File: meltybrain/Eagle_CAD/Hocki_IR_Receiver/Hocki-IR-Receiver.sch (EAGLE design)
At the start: 67 parts, among them U1 OPA2380AIDGKR, U10 LMH6612MAX/NOPB, U11 LMH6612MAX/NOPB, U2 OPA2380AIDGKR, U3 TLV3502AIDCNR, U4 TLV3502AIDCNR, U5 SN74LVC1G58DCKR, U6 NL27WZ32USG, U7 TMUX1204DGSR, U8 LP38693MP-5.0/NOPB, U9 TLV73310PDBVT

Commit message: progress...
IR receiver has all parts accounting BoM
started doing that for control
progress on control layout
Varun I hate this...
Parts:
- removed C4, C5: 50n, rcl:C-USC0603
- removed R5: 50, resistor:R-US_R0603
- C1: value 50n -> 47n; device rcl:C-USC0603 -> rcl:C-USC1206
- C2: value 0.5p -> 47n; device rcl:C-USC0603 -> rcl:C-USC1206
- C3: value 2p -> 47n; device rcl:C-USC0603 -> rcl:C-USC1206
- R1: device resistor:R-US_R0603 -> rcl:R-US_R1206
- R10, R11, R16, R21, R28, R29, R3, R30, R31, R4: value 500 -> 499
- R14, R15, R7: value 30k -> 31.6k
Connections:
- removed net N$11: C3.2, R13.1, R9.2, U2.OUTB
- removed net N$8: C2.2, R12.1, R8.2, U2.OUTA
- new net N$21: D1.A, R6.2
- net 100KGAIN: now also R12.1, R8.2, U2.OUTA; no longer D2.A, R12.2
- net 100KPEAK: now also C2.1; no longer C4.1
- net 10KGAIN: now also R13.1, R9.2, U2.OUTB; no longer D3.A, R13.2
- net 10KPEAK: now also C3.1; no longer C5.1
- net 10MGAIN: now also R1.2, U1.OUTA; no longer R5.2
- net 1MGAIN: now also R2.2, R6.1, U1.OUTB; no longer D1.A, R6.2
- net GND: now also C2.2, C3.2; no longer C4.2, C5.2
- net N$10: no longer C3.1
- net N$2: now also D2.A, R12.2; no longer R1.2, R5.1, U1.OUTA
- net N$4: now also D3.A, R13.2; no longer R2.2, R6.1, U1.OUTB
- net N$6: no longer C2.1
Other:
- moved on the sheet: C2, C3

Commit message: added IR connectors
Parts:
- added C4: 100p, rcl:C-USC0603
- added J1: SM05B-SRSS-TB(LF)(SN), Hocki_Library:SM05B-SRSS-TB(LF)(SN)
- C7: value 1u -> 2.2u
- U8: value LP38693MP-5.0/NOPB -> AP2210K-5.0TRG1; device Hocki_Library:LP38693MP-5.0/NOPB -> Hocki_Library:AP2210K-5.0TRG1
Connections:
- removed net VIN: C6.1, U8.EN, U8.VIN
- new net 9V: C6.1, J1.1, U8.EN, U8.IN
- new net N$8: C4.1, U8.BYP
- net 5V: now also J1.SHIELD, U8.OUT; no longer U8.VOUT
- net A0: now also J1.3
- net A1: now also J1.4
- net GND: now also C4.2, J1.5
- net VG_SIGNAL: now also J1.2

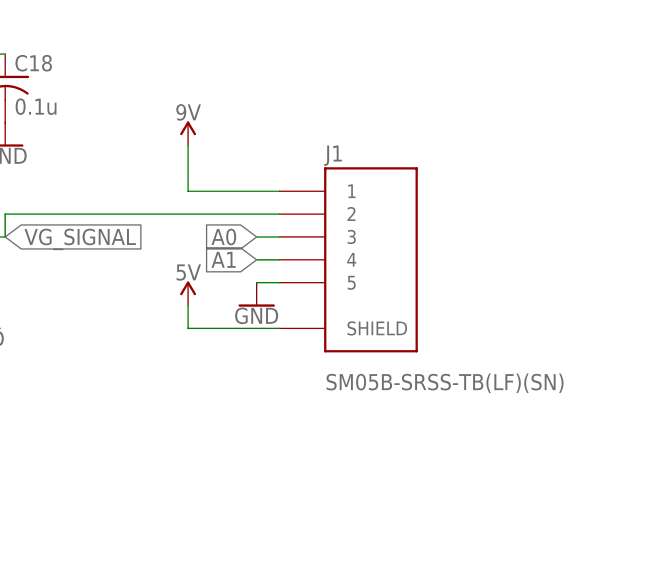
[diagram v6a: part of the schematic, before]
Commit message: 5 to 3 pin connector
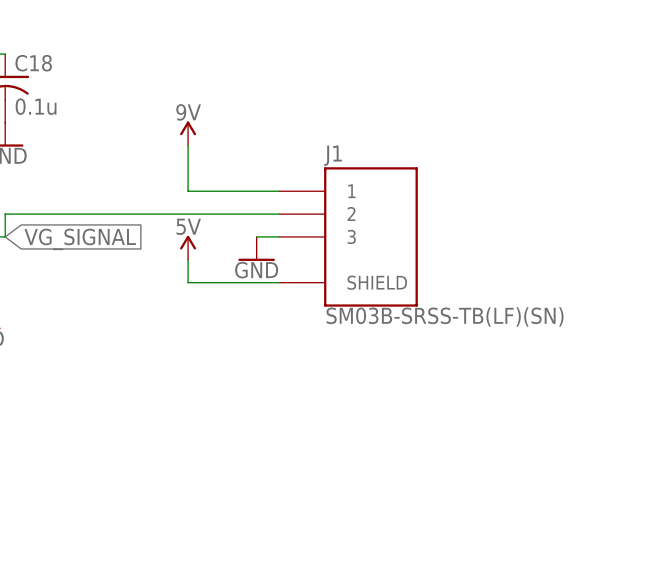
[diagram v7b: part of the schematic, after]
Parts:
- J1: value SM05B-SRSS-TB(LF)(SN) -> SM03B-SRSS-TB(LF)(SN); device Hocki_Library:SM05B-SRSS-TB(LF)(SN) -> Hocki_Library:SM03B-SRSS-TB(LF)(SN)
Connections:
- net A0: no longer J1.3
- net A1: no longer J1.4
- net GND: now also J1.3; no longer J1.5
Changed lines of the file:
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@@
 <part name="C4" library="rcl" library_urn="urn:adsk.eagle:library:334" deviceset="C-US" device="C0603" package3d_urn="urn:adsk.eagle:package:23616/2" value="100p"/>
 <part name="GND33" library="SparkFun-PowerSymbols" library_urn="urn:adsk.eagle:library:530" deviceset="GND" device=""/>
-<part name="J1" library="Hocki_Library" deviceset="SM05B-SRSS-TB(LF)(SN)" device=""/>
 <part name="SUPPLY12" library="Hocki_Library" deviceset="9V" device=""/>
 <part name="SUPPLY17" library="Hocki_Library" deviceset="9V" device=""/>
 <part name="GND34" library="SparkFun-PowerSymbols" library_urn="urn:adsk.eagle:library:530" deviceset="GND" device=""/>
 <part name="SUPPLY18" library="SparkFun-PowerSymbols" library_urn="urn:adsk.eagle:library:530" deviceset="5V" device=""/>
+<part name="J1" library="Hocki_Library" deviceset="SM03B-SRSS-TB(LF)(SN)" device=""/>
 </parts>
 <sheets>
@@
 <attribute name="VALUE" x="-30.48" y="63.246" size="1.778" layer="96" align="top-center"/>
 </instance>
-<instance part="J1" gate="G$1" x="347.98" y="5.08" smashed="yes">
-<attribute name="NAME" x="342.9" y="16.002" size="1.778" layer="95"/>
-<attribute name="VALUE" x="342.9" y="-7.62" size="1.778" layer="96" align="top-left"/>
-</instance>
 <instance part="SUPPLY12" gate="G$1" x="-63.5" y="91.44" smashed="yes">
 <attribute name="VALUE" x="-63.5" y="94.234" size="1.778" layer="96" align="bottom-center"/>
@@
 <attribute name="VALUE" x="327.66" y="20.574" size="1.778" layer="96" align="bottom-center"/>
 </instance>
-<instance part="GND34" gate="1" x="335.28" y="0" smashed="yes">
-<attribute name="VALUE" x="335.28" y="-0.254" size="1.778" layer="96" align="top-center"/>
-</instance>
-<instance part="SUPPLY18" gate="G$1" x="327.66" y="0" smashed="yes">
-<attribute name="VALUE" x="327.66" y="2.794" size="1.778" layer="96" align="bottom-center"/>
+<instance part="GND34" gate="1" x="335.28" y="5.08" smashed="yes">
+<attribute name="VALUE" x="335.28" y="4.826" size="1.778" layer="96" align="top-center"/>
+</instance>
+<instance part="SUPPLY18" gate="G$1" x="327.66" y="5.08" smashed="yes">
+<attribute name="VALUE" x="327.66" y="7.874" size="1.778" layer="96" align="bottom-center"/>
+</instance>
+<instance part="J1" gate="G$1" x="347.98" y="7.62" smashed="yes">
+<attribute name="NAME" x="342.9" y="16.002" size="1.778" layer="95"/>
+<attribute name="VALUE" x="342.9" y="-0.254" size="1.778" layer="96" align="top-left"/>
 </instance>
 </instances>
@@
 </segment>
 <segment>
-<pinref part="J1" gate="G$1" pin="5"/>
-<wire x1="337.82" y1="2.54" x2="335.28" y2="2.54" width="0.1524" layer="91"/>
 <pinref part="GND34" gate="1" pin="GND"/>
+<pinref part="J1" gate="G$1" pin="3"/>
+<wire x1="337.82" y1="7.62" x2="335.28" y2="7.62" width="0.1524" layer="91"/>
 </segment>
 </net>
@@
 </segment>
 <segment>
+<wire x1="337.82" y1="2.54" x2="327.66" y2="2.54" width="0.1524" layer="91"/>
+<pinref part="SUPPLY18" gate="G$1" pin="5V"/>
+<wire x1="327.66" y1="2.54" x2="327.66" y2="5.08" width="0.1524" layer="91"/>
 <pinref part="J1" gate="G$1" pin="SHIELD"/>
-<wire x1="337.82" y1="-2.54" x2="327.66" y2="-2.54" width="0.1524" layer="91"/>
-<pinref part="SUPPLY18" gate="G$1" pin="5V"/>
-<wire x1="327.66" y1="-2.54" x2="327.66" y2="0" width="0.1524" layer="91"/>
 </segment>
 </net>
@@
 <label x="266.7" y="0" size="1.778" layer="95" rot="R180" xref="yes"/>
 </segment>
-<segment>
-<pinref part="J1" gate="G$1" pin="4"/>
-<wire x1="337.82" y1="5.08" x2="335.28" y2="5.08" width="0.1524" layer="91"/>
-<label x="335.28" y="5.08" size="1.778" layer="95" rot="R180" xref="yes"/>
-</segment>
 </net>
 <net name="A0" class="0">
@@
 <wire x1="269.24" y1="2.54" x2="266.7" y2="2.54" width="0.1524" layer="91"/>
 <label x="266.7" y="2.54" size="1.778" layer="95" rot="R180" xref="yes"/>
-</segment>
-<segment>
-<pinref part="J1" gate="G$1" pin="3"/>
-<wire x1="337.82" y1="7.62" x2="335.28" y2="7.62" width="0.1524" layer="91"/>
-<label x="335.28" y="7.62" size="1.778" layer="95" rot="R180" xref="yes"/>
 </segment>
 </net>
@@
 <wire x1="302.26" y1="7.62" x2="307.34" y2="7.62" width="0.1524" layer="91"/>
 <label x="307.34" y="7.62" size="1.778" layer="95" xref="yes"/>
-<pinref part="J1" gate="G$1" pin="2"/>
 <wire x1="337.82" y1="10.16" x2="307.34" y2="10.16" width="0.1524" layer="91"/>
 <wire x1="307.34" y1="10.16" x2="307.34" y2="7.62" width="0.1524" layer="91"/>
+<pinref part="J1" gate="G$1" pin="2"/>
 </segment>
 </net>
@@
 </segment>
 <segment>
-<pinref part="J1" gate="G$1" pin="1"/>
 <wire x1="337.82" y1="12.7" x2="327.66" y2="12.7" width="0.1524" layer="91"/>
 <wire x1="327.66" y1="12.7" x2="327.66" y2="17.78" width="0.1524" layer="91"/>
 <pinref part="SUPPLY17" gate="G$1" pin="9V"/>
-</segment>
-</net>
+<pinref part="J1" gate="G$1" pin="1"/>
+</segment>
+</net>

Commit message: IR board 100%...again
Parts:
- removed C18: 0.1u, rcl:C-USC0603
- added C5: 47nF, rcl:C-USC1206
- added D8, D9: GREEN, SparkFun-LED:LED-GREEN0603
- added R32: 300, resistor:R-US_R0603
- added R5: 10M, rcl:R-US_R1206
- C1, C2: value 47n -> 1uF; device rcl:C-USC1206 -> rcl:C-USC0603
- C10: value 1u -> 2.2uF
- C11, C6: value 1u -> 1uF
- C12: value 0.1u -> 1uF
- C13, C14, C15, C16, C17: value 0.1u -> 0.1uF
- C3: value 47n -> 47nF
- C4: value 100p -> 47nF; device rcl:C-USC0603 -> rcl:C-USC1206
- C7: value 2.2u -> 100pF
- C8, C9: value 1u -> 0.1uF
- D1, D2, D3: value RB521S30T1G -> TEFD4300F; device Hocki_Library:RB521S30T1G -> Hocki_Library:TEFD4300F
- D5, D6, D7: value TEFD4300F -> RB521S30T1G; device Hocki_Library:TEFD4300F -> Hocki_Library:RB521S30T1G
- R1: value 10M -> 499; device rcl:R-US_R1206 -> resistor:R-US_R0603
- R10, R11: value 499 -> 49.9
- R12, R13: value 50 -> 31.6k
- R15: value 31.6k -> 499
- R16: value 499 -> 100
- R17: value 100 -> 30
- R18: value 300 -> 30
- R19: value 100 -> 300
- R2: value 1M -> 499
- R20: value 300 -> 100
- R21: value 499 -> 30
- R22: value 10k -> 300
- R25: value 30 -> 10k
- R26, R27: value 30 -> 499
- R6: value 50 -> 1M
- R7: value 31.6k -> 100k
- R8: value 100k -> 10k
- R9: value 10k -> 49.9
- U10: value LMH6612MAX/NOPB -> NL27WZ32USG; device Hocki_Library:LMH6612MAX/NOPB -> Hocki_Library:NL27WZ32USG
- U11: value LMH6612MAX/NOPB -> TMUX1204DGSR; device Hocki_Library:LMH6612MAX/NOPB -> Hocki_Library:TMUX1204DGSR
- U3: value TLV3502AIDCNR -> AP2210K-5.0TRG1; device Hocki_Library:TLV3502AIDCNR -> Hocki_Library:AP2210K-5.0TRG1
- U4: value TLV3502AIDCNR -> LMH6612MAX/NOPB; device Hocki_Library:TLV3502AIDCNR -> Hocki_Library:LMH6612MAX/NOPB
- U5: value SN74LVC1G58DCKR -> LMH6612MAX/NOPB; device Hocki_Library:SN74LVC1G58DCKR -> Hocki_Library:LMH6612MAX/NOPB
- U6: value NL27WZ32USG -> TLV73310PDBVT; device Hocki_Library:NL27WZ32USG -> Hocki_Library:TLV73310PDBVT
- U7: value TMUX1204DGSR -> TLV3502AIDCNR; device Hocki_Library:TMUX1204DGSR -> Hocki_Library:TLV3502AIDCNR
- U8: value AP2210K-5.0TRG1 -> TLV3502AIDCNR; device Hocki_Library:AP2210K-5.0TRG1 -> Hocki_Library:TLV3502AIDCNR
- U9: value TLV73310PDBVT -> SN74LVC1G58DCKR; device Hocki_Library:TLV73310PDBVT -> Hocki_Library:SN74LVC1G58DCKR
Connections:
- new net N$11: D9.C, R32.2
- new net N$24: D8.C, R31.2
- net 1.0V: now also C12.1, R1.2, R16.2, R20.2, U6.OUT; no longer C9.1, R10.2, R17.2, R19.2, U9.OUT
- net 100KGAIN: now also R11.1, R7.2, U11.S3; no longer R12.1, R8.2, U7.S3
- net 100KLOGIC: now also U10.B1, U7.OUTB, U9.IN1; no longer U3.OUTB, U5.IN1, U6.B1
- net 100KPEAK: now also C4.1, D6.C, R13.2, U4.INB+; no longer C2.1, D2.C, R14.2, U10.INB+
- net 10KGAIN: now also R10.1, R30.2, R8.2, U11.S4; no longer R13.1, R28.2, R9.2, U7.S4
- net 10KLOGIC: now also R25.1, U10.A1, U10.A2, U8.OUTA; no longer R23.1, U4.OUTA, U6.A1, U6.A2
- net 10KPEAK: now also C5.1, D7.C, R14.2, U5.INA+; no longer C3.1, D3.C, R15.2, U11.INA+
- net 10MGAIN: now also R27.2, R5.2, U11.S1; no longer R1.2, R31.2, U7.S1
- net 1MGAIN: now also R28.2, R6.2, R9.1, U11.S2; no longer R2.2, R30.2, R6.1, U7.S2
- net 1MLOGIC: now also R23.1, U7.OUTA, U9.IN2; no longer R22.1, U3.OUTA, U5.IN2
- net 5V: now also C1.1, C2.1, C9.1, D9.A, U10.VCC, U11.EN, U11.VCC, U3.OUT, U5.V+, U6.EN, U6.IN, U7.V+, U8.V+, U9.VCC; no longer C12.1, C18.1, C7.1, U10.V+, U11.V+, U3.V+, U5.VCC, U6.VCC, U7.EN, U7.VCC, U8.OUT, U9.EN, U9.IN
- net 9V: now also D8.A, U3.EN, U3.IN; no longer U8.EN, U8.IN
- net A0: now also U10.Y2, U11.A0; no longer U6.Y2, U7.A0
- net A1: now also U10.Y1, U11.A1; no longer U6.Y1, U7.A1
- net GND: now also C5.2, D1.ANODE, D2.ANODE, D3.ANODE, R12.1, R13.1, R19.1, R2.1, R22.1, R26.1, R27.1, R32.1, U10.GND, U11.GND, U3.GND, U5.INB+, U5.INB-, U5.V-, U7.V-, U8.INB-, U8.V-, U9.IN0; no longer C18.2, D5.ANODE, D6.ANODE, D7.ANODE, R11.1, R16.1, R18.1, R20.1, R21.1, R7.1, U10.V-, U11.INB+, U11.INB-, U11.V-, U3.V-, U4.INB-, U5.GND, U5.IN0, U7.GND, U8.GND
- net N$1: now also D1.CATHODE, R5.1; no longer D4.CATHODE, R1.1
- net N$10: now also D4.CATHODE, R8.1; no longer D7.CATHODE, R9.1
- net N$12: now also R3.1, R4.2; no longer R10.1, R11.2
- net N$13: now also R20.1, R22.2, U7.INA-, U7.INB-; no longer R17.1, R18.2, U3.INA-, U3.INB-
- net N$14: now also R16.1, R19.2, U8.INA-, U8.INB+; no longer R19.1, R20.2, U4.INA-, U4.INB+
- net N$15: now also R21.1, U5.INA-, U5.OUTA; no longer R27.1, U11.INA-, U11.OUTA
- net N$16: now also R17.1, U4.INA-, U4.OUTA; no longer R25.1, U10.INA-, U10.OUTA
- net N$17: now also C3.1, D5.C, R12.2, U4.INA+; no longer C1.1, D1.C, R7.2, U10.INA+
- net N$18: now also R18.1, U4.INB-, U4.OUTB; no longer R26.1, U10.INB-, U10.OUTB
- net N$19: now also R15.2, U5.OUTB; no longer R21.2, U11.OUTB
- net N$2: now also D6.A, R11.2; no longer D2.A, R12.2
- net N$20: now also R18.2, U7.INB+; no longer R26.2, U3.INB+
- net N$21: now also D5.A, R9.2; no longer D1.A, R6.2
- net N$22: now also R21.2, R25.2, U8.INA+; no longer R23.2, R27.2, U4.INA+
- net N$23: now also R17.2, R23.2, U7.INA+; no longer R22.2, R25.2, U3.INA+
- net N$3: now also D3.CATHODE, R6.1; no longer D5.CATHODE, R2.1
- net N$4: now also D7.A, R10.2; no longer D3.A, R13.2
- net N$5: now also R1.1, R2.2; no longer R3.1, R4.2
- net N$6: now also D2.CATHODE, R7.1; no longer D6.CATHODE, R8.1
- net N$7: now also R26.2, U8.OUTB; no longer R16.2, U4.OUTB
- net N$8: now also C7.1, U3.BYP; no longer C4.1, U8.BYP
- net N$9: now also U10.B2, U9.Y; no longer U5.Y, U6.B2
- net VG_SIGNAL: now also U11.D; no longer U7.D
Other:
- moved on the sheet: C1, C10, C11, C12, C13, C14, C15, C16, C17, C2, C3, C4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
